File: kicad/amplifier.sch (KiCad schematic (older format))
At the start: 21 parts, among them U6 GS8332-SR

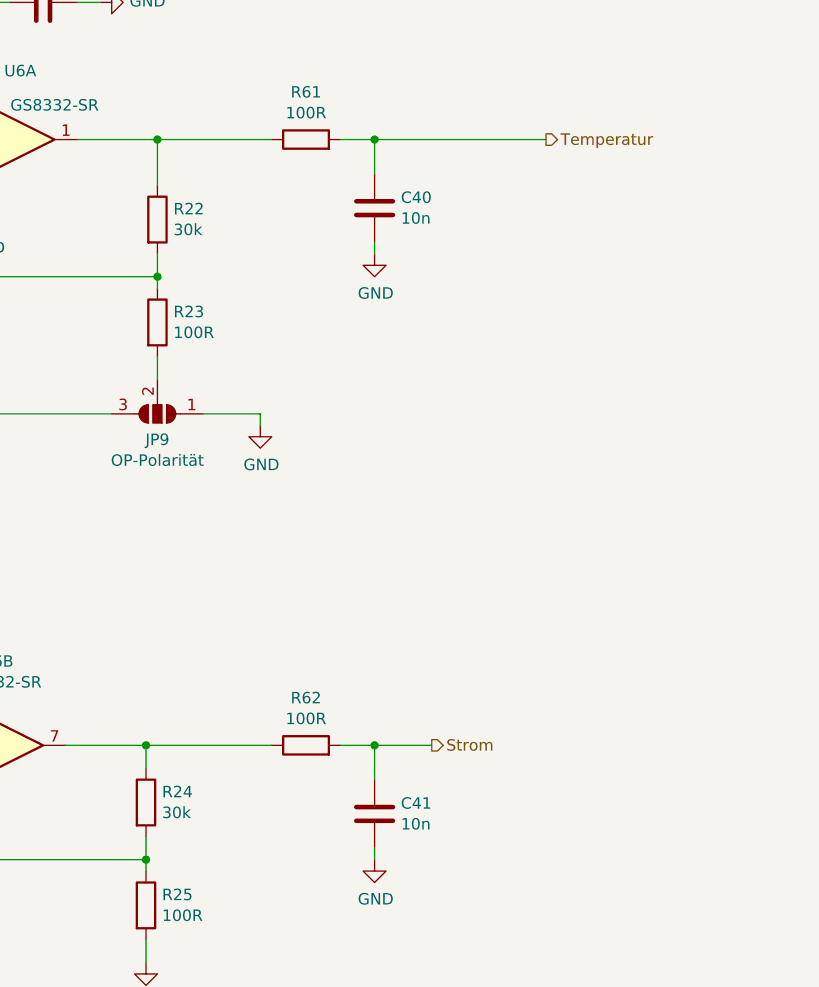
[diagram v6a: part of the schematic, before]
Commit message: Hardware-Anpassungen bei Inbetriebnahme und Firmwareaktualisierung
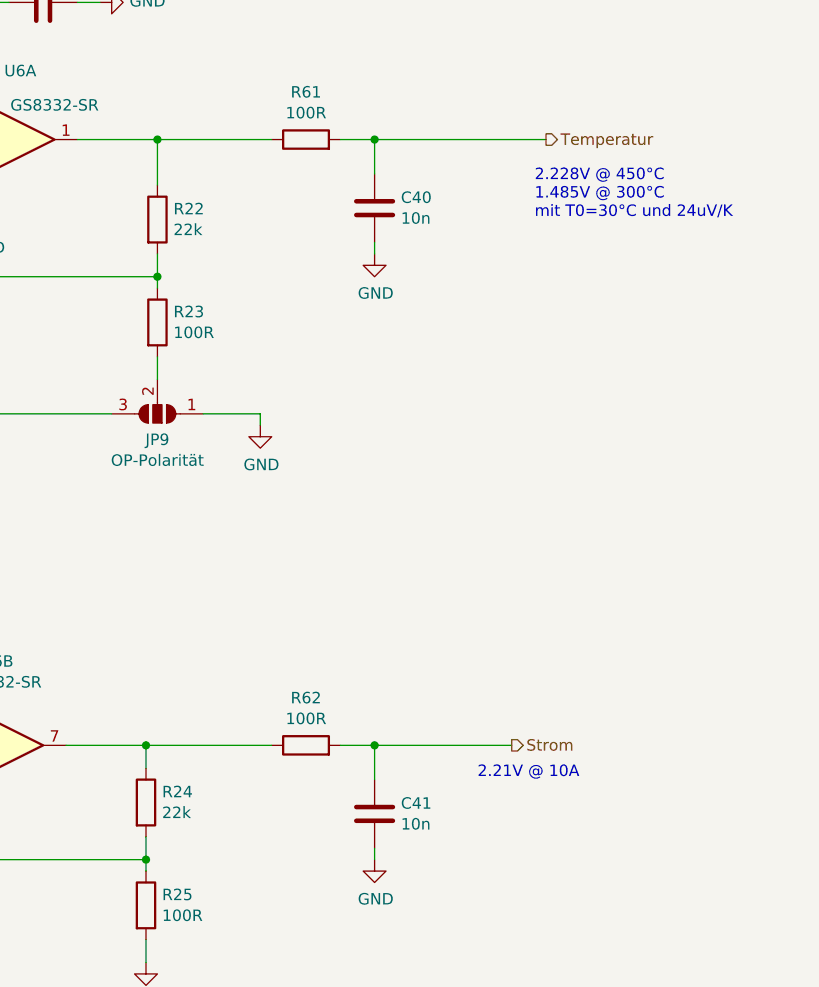
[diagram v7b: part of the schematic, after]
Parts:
- R22, R24: value 30k -> 22k
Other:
- note added: "2.21V @ 10A"
- note added: "2.228V @ 450°C\n1.485V @ 300°C\nmit T0=30°C und 24uV/K"
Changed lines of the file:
@@
 P 7200 3050
 F 0 "R22" H 7270 3096 50  0000 L CNN
-F 1 "30k" H 7270 3005 50  0000 L CNN
+F 1 "22k" H 7270 3005 50  0000 L CNN
 F 2 "Resistor_SMD:R_1206_3216Metric" V 7130 3050 50  0001 C CNN
 F 3 "~" H 7200 3050 50  0001 C CNN
@@
 P 7150 5600
 F 0 "R24" H 7220 5646 50  0000 L CNN
-F 1 "30k" H 7220 5555 50  0000 L CNN
+F 1 "22k" H 7220 5555 50  0000 L CNN
 F 2 "Resistor_SMD:R_1206_3216Metric" V 7080 5600 50  0001 C CNN
 F 3 "~" H 7150 5600 50  0001 C CNN
@@
 	7150 5350 7700 5350
 Connection ~ 7150 5350
-Text HLabel 8400 5350 2    50   Output ~ 0
+Text HLabel 8750 5350 2    50   Output ~ 0
 Strom
 $Comp
@@
 Connection ~ 8150 5350
 Wire Wire Line
-	8150 5350 8400 5350
+	8150 5350 8750 5350
 Text Notes 5700 1600 0    50   ~ 0
 Polarität des Verstärkers wählbar:\n1-2: für positive Eingangsspannungen\n2-3: für negative Eingangsspannungen
+Text Notes 8850 3050 0    50   ~ 0
+2.228V @ 450°C\n1.485V @ 300°C\nmit T0=30°C und 24uV/K
+Text Notes 8600 5500 0    50   ~ 0
+2.21V @ 10A
 $EndSCHEMATC

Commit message: HTML-BOM aktualisiert
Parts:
- R22, R24: DistOrderNr C137314 -> (none)
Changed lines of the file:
@@
 F 3 "~" H 7200 3050 50  0001 C CNN
 F 4 "0.01" H 7200 3050 50  0001 C CNN "PriceEUR"
-F 5 "C137314" H 7200 3050 50  0001 C CNN "DistOrderNr"
-F 6 "LCSC" H 7200 3050 50  0001 C CNN "Distributor"
+F 5 "LCSC" H 7200 3050 50  0001 C CNN "Distributor"
 	1    7200 3050
 	1    0    0    -1
@@
 F 3 "~" H 7150 5600 50  0001 C CNN
 F 4 "0.01" H 7150 5600 50  0001 C CNN "PriceEUR"
-F 5 "C137314" H 7150 5600 50  0001 C CNN "DistOrderNr"
-F 6 "LCSC" H 7150 5600 50  0001 C CNN "Distributor"
+F 5 "LCSC" H 7150 5600 50  0001 C CNN "Distributor"
 	1    7150 5600
 	1    0    0    -1
